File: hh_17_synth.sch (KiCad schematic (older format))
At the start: 31 parts, among them J1 USB_OTG, J2 debug, J3 JACK_TRS, SW1 SW_Push, U1 LM1117-3.3, U2 STM32F072CBTx, Y1 16MHz

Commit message: finished layout etc.
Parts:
- J3: Manufacturer (none) -> tayda electronics; Mfg_Part_No (none) -> http://www.taydaelectronics.com/review/product/list/id/2876/; alternate (none) -> 490-SJ1-3525N mouser
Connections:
- net DAC_C1: now also R2.2; no longer R3.2
- net DAC_C2: now also R3.2; no longer R2.2
- net VDD: now also SW1.2
- net USB_DM renamed USB_D_N
- net USB_DP renamed USB_D_P
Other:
- note added: "TODO\n=====\nbattery connector?\nspeaker connecter/audio amp?\npotentiometers?\nrf module?"
- note added: "will not need an audio amplifier\nat least for headphones\nmcu has built in buffer driver\n0.2V to Vdd-0.3V"
- note removed: "will not need an audio amplifier\nmcu has built in buffer driver\n0.2V to Vdd-0.3V"
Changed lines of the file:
@@
 VBUS
 Text Label 12940 1840 0    60   ~ 0
-USB_DM
+USB_D_N
 Text Label 12940 1740 0    60   ~ 0
-USB_DP
+USB_D_P
 NoConn ~ 12715 1940
 $Comp
@@
 $EndComp
 Text Label 11710 4885 0    60   ~ 0
-USB_DM
+USB_D_N
 Text Label 11710 4985 0    60   ~ 0
-USB_DP
+USB_D_P
 $Comp
 L LM1117-3.3 U1
@@
 Text Label 14020 2955 0    60   ~ 0
 BOOT0
-Text Label 15330 2940 0    60   ~ 0
+Text Label 15345 2955 0    60   ~ 0
 VDD
 $Comp
@@
 DAC_C2
 Text Notes 5060 6525 0    60   ~ 0
-will not need an audio amplifier\nmcu has built in buffer driver\n0.2V to Vdd-0.3V
+will not need an audio amplifier\nat least for headphones\nmcu has built in buffer driver\n0.2V to Vdd-0.3V
 $Comp
 L JACK_TRS J3
@@
 F 2 "custom:Tayda_3.5mm_stereo_TRS_jack_A-853" H 7235 7020 50  0001 C CNN
 F 3 "" H 7235 7020 50  0000 C CNN
+F 4 "http://www.taydaelectronics.com/review/product/list/id/2876/" H 7235 7020 60  0001 C CNN "Mfg_Part_No"
+F 5 "tayda electronics" H 7235 7020 60  0001 C CNN "Manufacturer"
+F 6 "490-SJ1-3525N  mouser" H 7235 7020 60  0001 C CNN "alternate"
 	1    7235 7020
 	-1   0    0    1
@@
 	1    0    0    -1
 $EndComp
+Text Label 3555 6860 2    60   ~ 0
+DAC_C2
 Text Label 3530 7535 2    60   ~ 0
-DAC_C2
-Text Label 3555 6860 2    60   ~ 0
 DAC_C1
 $Comp
@@
 	14420 3080 14420 2955
 Wire Wire Line
-	15330 2940 15055 2940
+	15345 2955 15070 2955
 Wire Wire Line
 	14020 2955 14670 2955
@@
 Text Notes 13700 2725 0    60   ~ 0
 TODO: choose button and verify button footprint
+Text Notes 1040 5175 0    60   ~ 0
+TODO\n=====\nbattery connector?\nspeaker connecter/audio amp?\npotentiometers?\nrf module?
 $EndSCHEMATC

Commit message: update todo
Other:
- note added: "TODO\n=====\nbattery connector\n2 potentiometers"
- note removed: "TODO\n=====\nbattery connector?\nspeaker connecter/audio amp?\npotentiometers?\nrf module?"
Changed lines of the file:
@@
 TODO: choose button and verify button footprint
 Text Notes 1040 5175 0    60   ~ 0
-TODO\n=====\nbattery connector?\nspeaker connecter/audio amp?\npotentiometers?\nrf module?
+TODO\n=====\nbattery connector\n2 potentiometers
 $EndSCHEMATC

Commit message: updated layout with buttons/pots
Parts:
- added R5, R6: 10k, Resistors_SMD:R_0603, symbol R
- added RV1, RV2: POT, custom:3386P-1-T, symbol POT
- added SW2, SW3: SW_Push, Buttons_Switches_THT:SW_PUSH_6mm, symbol SW_Push
- C5, C6: footprint Capacitors_ThroughHole:CP_Radial_D5.0mm_P2.00mm -> Capacitors_THT:CP_Radial_D5.0mm_P2.00mm
- SW1: footprint Buttons_Switches_ThroughHole:SW_PUSH_6mm -> Buttons_Switches_THT:SW_PUSH_6mm
- renumbered J2 to SWD1
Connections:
- net A: now also U2.27 (PB14/I2C2_SDA/I2S2_MCK/SPI2_MISO/TIM15_CH1/TIM1_CH2N/TSC_G6_IO4/USART3_DE/USART3_RTS); no longer U2.19 (PB1/ADC_IN9/TIM14_CH1/TIM1_CH3N/TIM3_CH4/TSC_G3_IO3/USART3_DE/USART3_RTS)
- net G#: now also U2.26 (PB13/I2C2_SCL/I2S2_CK/SPI2_SCK/TIM1_CH1N/TSC_G6_IO3/USART3_CTS); no longer U2.18 (PB0/ADC_IN8/TIM1_CH2N/TIM3_CH3/TSC_G3_IO2/USART3_CK)
- net GND: now also R5.2, R6.2, RV1.3, RV2.3
- net TB1: now also U2.22 (PB11/I2C2_SDA/TIM2_CH4/TSC_G6_IO1/USART3_RX); no longer U2.42 (PB6/I2C1_SCL/TIM16_CH1N/TSC_G5_IO3/USART1_TX)
- net TB2: now also U2.25 (PB12/I2S2_WS/SPI2_NSS/TIM15_BKIN/TIM1_BKIN/TSC_G6_IO2/USART3_CK); no longer U2.43 (PB7/I2C1_SDA/TIM17_CH1N/TSC_G5_IO4/USART1_RX/USART4_CTS)
- net VDD: now also RV1.1, RV2.1, SW2.2, SW3.2
- net PB1: now reaches U2.41 (PB5/I2C1_SMBA/I2S1_SD/SPI1_MOSI/SYS_WKUP6/TIM16_BKIN/TIM3_CH2)
- net PB1: now also R5.1, SW2.1
- new net PB2: R6.1, SW3.1, U2.42 (PB6/I2C1_SCL/TIM16_CH1N/TSC_G5_IO3/USART1_TX)
- new net PT1: RV1.2, U2.18 (PB0/ADC_IN8/TIM1_CH2N/TIM3_CH3/TSC_G3_IO2/USART3_CK)
- new net PT2: RV2.2, U2.19 (PB1/ADC_IN9/TIM14_CH1/TIM1_CH3N/TIM3_CH4/TSC_G3_IO3/USART3_DE/USART3_RTS)
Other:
- note added: "TODO\n=====\nbattery connector"
- note removed: "TODO\n=====\nbattery connector\n2 potentiometers"
- note removed: "http://www.taydaelectronics.com/review/product/list/id/2876/"

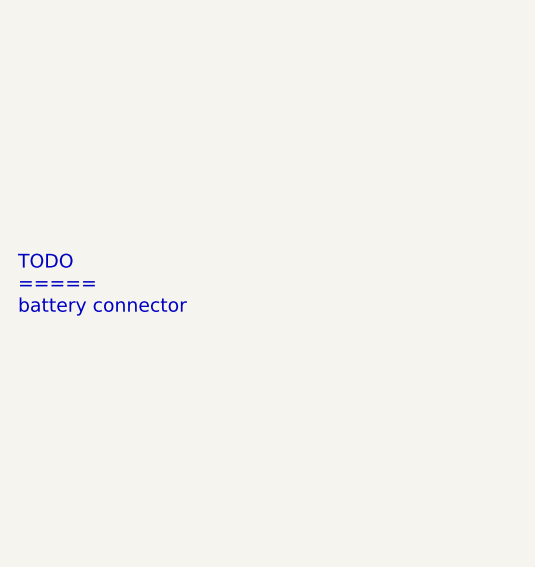
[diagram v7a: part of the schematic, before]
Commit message: minor: doc update
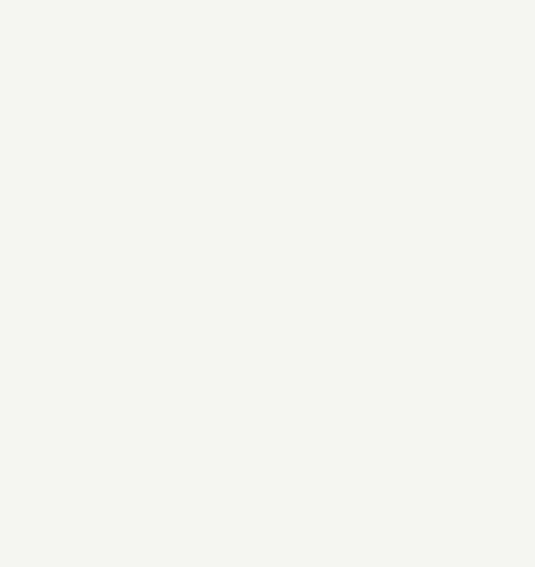
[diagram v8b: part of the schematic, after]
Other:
- note removed: "TODO\n=====\nbattery connector"
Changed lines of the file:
@@
 Text Notes 13700 2725 0    60   ~ 0
 TODO: choose button and verify button footprint
-Text Notes 1040 5175 0    60   ~ 0
-TODO\n=====\nbattery connector
 $Comp
 L PWR_FLAG #FLG017
